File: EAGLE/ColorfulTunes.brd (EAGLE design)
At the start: 160 x 100 mm, 6 parts, among them U1 0.56_HEX_BACKPACK

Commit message: Please check this schematic :)
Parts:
- added CS1: COLOR_SENSOR_PINS, ColorfulTunes:COLOR_SENSOR
- added R4, R5, R6, R7: (no value), ColorfulTunes:R0402
- added R8: POTENTIOMETER, ColorfulTunes:POT-PO90S
- added SERVO1: SERVO_PINS, ColorfulTunes:SERVO_PINS
- added USB1: USB_BOI, ColorfulTunes:USB_BOI
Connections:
- removed net RGB_PWR: D1.1, U$1.59
- removed net SYS.5V: U$1.24
- removed net SYS.5V_1: U$1.49
- removed net SYS.GND_1: U$1.22
- removed net SYS.GND_3: U$1.51
- removed net SYS_VIN: U$1.1
- removed net VCC: U1.VCC
- new net AIN_1V8.0: R8.S, U$1.19
- new net AIN_1V8.REF+: R8.CCW, U$1.18
- new net AIN_1V8.REF-: R8.CW, U$1.17
- new net GND: CS1.GND, SERVO1.P$1, U$1.16, U$1.22, U$1.51, U$1.57, U1.GND
- new net I2C1.SCL: CS1.SCL, R7.1, U$1.45
- new net I2C1.SDA: CS1.SDA, R6.1, U$1.47
- new net I2C2.SCL: R4.1, U$1.28, U1.SCL
- new net I2C2.SDA: R5.1, U$1.26, U1.SDA
- new net N$4: U$1.3, U$1.5
- new net SERVO_PWM: SERVO1.P$3, U$1.36
- new net USB1.D+: U$1.11, USB1.D+
- new net USB1.D-: U$1.9, USB1.D-
- new net USB1.GND: U$1.13, U$1.15, USB1.GND
- new net USB1.VIN: U$1.7, USB1.5V
- new net VDD_3P3V: D1.1, R4.2, R5.2, R6.2, R7.2, U$1.14, U$1.59
- new net VDD_5V: CS1.VIN, SERVO1.P$2, U$1.1, U$1.24, U$1.49, U1.VCC
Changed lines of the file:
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@@
 <attribute name="VALUE" x="-60.96" y="38.1" size="1.27" layer="27"/>
 </element>
+<element name="R4" library="ColorfulTunes" package="R0402" value="" x="-68.58" y="-2.54" smashed="yes">
+<attribute name="NAME" x="-69.469" y="-2.032" size="0.8128" layer="25"/>
+<attribute name="VALUE" x="-69.469" y="-3.302" size="0.254" layer="27"/>
+</element>
+<element name="R5" library="ColorfulTunes" package="R0402" value="" x="-68.58" y="-6.35" smashed="yes">
+<attribute name="NAME" x="-69.469" y="-5.842" size="0.8128" layer="25"/>
+<attribute name="VALUE" x="-69.469" y="-7.112" size="0.254" layer="27"/>
+</element>
+<element name="CS1" library="ColorfulTunes" package="COLOR_SENSOR" value="COLOR_SENSOR_PINS" x="-67.31" y="-10.16" smashed="yes"/>
+<element name="R6" library="ColorfulTunes" package="R0402" value="" x="-68.58" y="-13.97" smashed="yes">
+<attribute name="NAME" x="-69.469" y="-13.462" size="0.8128" layer="25"/>
+<attribute name="VALUE" x="-69.469" y="-14.732" size="0.254" layer="27"/>
+</element>
+<element name="R7" library="ColorfulTunes" package="R0402" value="" x="-68.58" y="-17.78" smashed="yes">
+<attribute name="NAME" x="-69.469" y="-17.272" size="0.8128" layer="25"/>
+<attribute name="VALUE" x="-69.469" y="-18.542" size="0.254" layer="27"/>
+</element>
+<element name="USB1" library="ColorfulTunes" package="USB_BOI" value="USB_BOI" x="-80.01" y="-2.54" smashed="yes">
+<attribute name="NAME" x="-84.54" y="2.68" size="1.778" layer="25" font="vector" ratio="12"/>
+<attribute name="VALUE" x="-84.6" y="-18.18" size="1.778" layer="27" font="vector" ratio="12"/>
+</element>
+<element name="R8" library="ColorfulTunes" package="POT-PO90S" value="POTENTIOMETER" x="-95.25" y="-15.24" smashed="yes">
+<attribute name="NAME" x="-100.33" y="-2.54" size="0.8128" layer="25"/>
+<attribute name="VALUE" x="-100.33" y="-17.78" size="0.8128" layer="27"/>
+</element>
+<element name="SERVO1" library="ColorfulTunes" package="SERVO_PINS" value="SERVO_PINS" x="-96.52" y="-20.32" smashed="yes"/>
 </elements>
 <signals>
-<signal name="SYS_VIN">
-<contactref element="U$1" pad="1"/>
-</signal>
-<signal name="SYS.GND_1">
-<contactref element="U$1" pad="22"/>
-</signal>
-<signal name="SYS.5V">
-<contactref element="U$1" pad="24"/>
-</signal>
-<signal name="SYS.GND_3">
-<contactref element="U$1" pad="51"/>
-</signal>
-<signal name="SYS.5V_1">
-<contactref element="U$1" pad="49"/>
-</signal>
-<signal name="VCC">
-<contactref element="U1" pad="VCC"/>
-</signal>
-<signal name="RGB_PWR">
-<contactref element="D1" pad="1"/>
-<contactref element="U$1" pad="59"/>
-<wire x1="-35.814" y1="29.21" x2="-66.81" y2="43.17" width="0" layer="19" extent="1-1"/>
-</signal>
 <signal name="N$1">
 <contactref element="R1" pad="1"/>
@@
 <wire x1="-51.5112" y1="71.12" x2="-61.214" y2="29.21" width="0" layer="19" extent="1-1"/>
 </signal>
+<signal name="VDD_3P3V">
+<contactref element="D1" pad="1"/>
+<contactref element="R4" pad="2"/>
+<contactref element="U$1" pad="59"/>
+<contactref element="U$1" pad="14"/>
+<contactref element="R5" pad="2"/>
+<contactref element="R6" pad="2"/>
+<contactref element="R7" pad="2"/>
+<wire x1="-68.0212" y1="-13.97" x2="-68.0212" y2="-17.78" width="0" layer="19" extent="1-1"/>
+<wire x1="-68.0212" y1="-6.35" x2="-68.0212" y2="-13.97" width="0" layer="19" extent="1-1"/>
+<wire x1="-68.0212" y1="-2.54" x2="-68.0212" y2="-6.35" width="0" layer="19" extent="1-1"/>
+<wire x1="-48.514" y1="9.398" x2="-68.0212" y2="-2.54" width="0" layer="19" extent="1-1"/>
+<wire x1="-35.814" y1="29.21" x2="-48.514" y2="9.398" width="0" layer="19" extent="1-1"/>
+<wire x1="-66.81" y1="43.17" x2="-35.814" y2="29.21" width="0" layer="19" extent="1-1"/>
+</signal>
+<signal name="VDD_5V">
+<contactref element="U1" pad="VCC"/>
+<contactref element="U$1" pad="24"/>
+<contactref element="U$1" pad="49"/>
+<contactref element="U$1" pad="1"/>
+<contactref element="CS1" pad="VIN"/>
+<contactref element="SERVO1" pad="P$2"/>
+<wire x1="-63.754" y1="6.858" x2="-96.52" y2="-20.32" width="0" layer="19" extent="1-1"/>
+<wire x1="-52.07" y1="-10.16" x2="-63.754" y2="6.858" width="0" layer="19" extent="1-1"/>
+<wire x1="-35.814" y1="9.398" x2="-52.07" y2="-10.16" width="0" layer="19" extent="1-1"/>
+<wire x1="-48.514" y1="29.21" x2="-35.814" y2="9.398" width="0" layer="19" extent="1-1"/>
+<wire x1="-34.036" y1="64.77" x2="-48.514" y2="29.21" width="0" layer="19" extent="1-1"/>
+</signal>
+<signal name="I2C2.SCL">
+<contactref element="U$1" pad="28"/>
+<contactref element="R4" pad="1"/>
+<contactref element="U1" pad="SCL"/>
+<wire x1="-30.734" y1="9.398" x2="-69.1388" y2="-2.54" width="0" layer="19" extent="1-1"/>
+<wire x1="-41.656" y1="64.77" x2="-30.734" y2="9.398" width="0" layer="19" extent="1-1"/>
+</signal>
+<signal name="I2C2.SDA">
+<contactref element="U$1" pad="26"/>
+<contactref element="U1" pad="SDA"/>
+<contactref element="R5" pad="1"/>
+<wire x1="-33.274" y1="9.398" x2="-69.1388" y2="-6.35" width="0" layer="19" extent="1-1"/>
+<wire x1="-39.116" y1="64.77" x2="-33.274" y2="9.398" width="0" layer="19" extent="1-1"/>
+</signal>
+<signal name="GND">
+<contactref element="U$1" pad="57"/>
+<contactref element="U$1" pad="16"/>
+<contactref element="U$1" pad="51"/>
+<contactref element="U$1" pad="22"/>
+<contactref element="U1" pad="GND"/>
+<contactref element="CS1" pad="GND"/>
+<contactref element="SERVO1" pad="P$1"/>
+<wire x1="-54.61" y1="-10.16" x2="-99.06" y2="-20.32" width="0" layer="19" extent="1-1"/>
+<wire x1="-45.974" y1="9.398" x2="-54.61" y2="-10.16" width="0" layer="19" extent="1-1"/>
+<wire x1="-38.354" y1="9.398" x2="-45.974" y2="9.398" width="0" layer="19" extent="1-1"/>
+<wire x1="-45.974" y1="29.21" x2="-45.974" y2="9.398" width="0" layer="19" extent="1-1"/>
+<wire x1="-38.354" y1="29.21" x2="-45.974" y2="29.21" width="0" layer="19" extent="1-1"/>
+<wire x1="-36.576" y1="64.77" x2="-38.354" y2="29.21" width="0" layer="19" extent="1-1"/>
+</signal>
+<signal name="I2C1.SDA">
+<contactref element="CS1" pad="SDA"/>
+<contactref element="R6" pad="1"/>
+<contactref element="U$1" pad="47"/>
+<wire x1="-62.23" y1="-10.16" x2="-69.1388" y2="-13.97" width="0" layer="19" extent="1-1"/>
+<wire x1="-51.054" y1="29.21" x2="-62.23" y2="-10.16" width="0" layer="19" extent="1-1"/>
+</signal>
+<signal name="I2C1.SCL">
+<contactref element="CS1" pad="SCL"/>
+<contactref element="R7" pad="1"/>
+<contactref element="U$1" pad="45"/>
+<wire x1="-59.69" y1="-10.16" x2="-69.1388" y2="-17.78" width="0" layer="19" extent="1-1"/>
+<wire x1="-53.594" y1="29.21" x2="-59.69" y2="-10.16" width="0" layer="19" extent="1-1"/>
+</signal>
+<signal name="USB1.GND">
+<contactref element="USB1" pad="GND"/>
+<contactref element="U$1" pad="13"/>
+<contactref element="U$1" pad="15"/>
+<wire x1="-48.514" y1="6.858" x2="-76.51" y2="-2.54" width="0" layer="19" extent="1-1"/>
+<wire x1="-45.974" y1="6.858" x2="-48.514" y2="6.858" width="0" layer="19" extent="1-1"/>
+</signal>
+<signal name="USB1.D+">
+<contactref element="USB1" pad="D+"/>
+<contactref element="U$1" pad="11"/>
+<wire x1="-51.054" y1="6.858" x2="-79.01" y2="-2.54" width="0" layer="19" extent="1-1"/>
+</signal>
+<signal name="USB1.D-">
+<contactref element="USB1" pad="D-"/>
+<contactref element="U$1" pad="9"/>
+<wire x1="-53.594" y1="6.858" x2="-81.01" y2="-2.54" width="0" layer="19" extent="1-1"/>
+</signal>
+<signal name="USB1.VIN">
+<contactref element="USB1" pad="5V"/>
+<contactref element="U$1" pad="7"/>
+<wire x1="-56.134" y1="6.858" x2="-83.51" y2="-2.54" width="0" layer="19" extent="1-1"/>
+</signal>
+<signal name="N$4">
+<contactref element="U$1" pad="3"/>
+<contactref element="U$1" pad="5"/>
+<wire x1="-58.674" y1="6.858" x2="-61.214" y2="6.858" width="0" layer="19" extent="1-1"/>
+</signal>
+<signal name="AIN_1V8.0">
+<contactref element="R8" pad="S"/>
+<contactref element="U$1" pad="19"/>
+<wire x1="-40.894" y1="6.858" x2="-95.25" y2="-15.24" width="0" layer="19" extent="1-1"/>
+</signal>
+<signal name="AIN_1V8.REF+">
+<contactref element="R8" pad="CCW"/>
+<contactref element="U$1" pad="18"/>
+<wire x1="-43.434" y1="9.398" x2="-97.75" y2="-15.24" width="0" layer="19" extent="1-1"/>
+</signal>
+<signal name="AIN_1V8.REF-">
+<contactref element="R8" pad="CW"/>
+<contactref element="U$1" pad="17"/>
+<wire x1="-43.434" y1="6.858" x2="-92.75" y2="-15.24" width="0" layer="19" extent="1-1"/>
+</signal>
+<signal name="SERVO_PWM">
+<contactref element="SERVO1" pad="P$3"/>
+<contactref element="U$1" pad="36"/>
+<wire x1="-20.574" y1="9.398" x2="-93.98" y2="-20.32" width="0" layer="19" extent="1-1"/>
+</signal>
 </signals>

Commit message: Found some mistakes, please check this one. Thank you!
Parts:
- R1, R2, R3: value (none) -> 470 M
- R4, R6, R7: value (none) -> 2.2 k
- R5: value (none) -> 2.2k
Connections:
- new net SYS.5V_1: U$1.49
- net VDD_5V: no longer U$1.49
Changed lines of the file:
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@@
 <attribute name="VALUE" x="-68.31" y="37.67" size="0.8128" layer="27" font="vector" ratio="12"/>
 </element>
-<element name="R1" library="ColorfulTunes" package="R0402" value="" x="-46.99" y="71.12" smashed="yes">
+<element name="R1" library="ColorfulTunes" package="R0402" value="470 M" x="-46.99" y="71.12" smashed="yes">
 <attribute name="NAME" x="-47.879" y="71.628" size="0.8128" layer="25"/>
 <attribute name="VALUE" x="-47.879" y="70.358" size="0.254" layer="27"/>
 </element>
-<element name="R2" library="ColorfulTunes" package="R0402" value="" x="-49.53" y="71.12" smashed="yes">
+<element name="R2" library="ColorfulTunes" package="R0402" value="470 M" x="-49.53" y="71.12" smashed="yes">
 <attribute name="NAME" x="-50.419" y="71.628" size="0.8128" layer="25"/>
 <attribute name="VALUE" x="-50.419" y="70.358" size="0.254" layer="27"/>
 </element>
-<element name="R3" library="ColorfulTunes" package="R0402" value="" x="-52.07" y="71.12" smashed="yes">
+<element name="R3" library="ColorfulTunes" package="R0402" value="470 M" x="-52.07" y="71.12" smashed="yes">
 <attribute name="NAME" x="-52.959" y="71.628" size="0.8128" layer="25"/>
 <attribute name="VALUE" x="-52.959" y="70.358" size="0.254" layer="27"/>
@@
 <attribute name="VALUE" x="-60.96" y="38.1" size="1.27" layer="27"/>
 </element>
-<element name="R4" library="ColorfulTunes" package="R0402" value="" x="-68.58" y="-2.54" smashed="yes">
+<element name="R4" library="ColorfulTunes" package="R0402" value="2.2 k" x="-68.58" y="-2.54" smashed="yes">
 <attribute name="NAME" x="-69.469" y="-2.032" size="0.8128" layer="25"/>
 <attribute name="VALUE" x="-69.469" y="-3.302" size="0.254" layer="27"/>
 </element>
-<element name="R5" library="ColorfulTunes" package="R0402" value="" x="-68.58" y="-6.35" smashed="yes">
+<element name="R5" library="ColorfulTunes" package="R0402" value="2.2k" x="-68.58" y="-6.35" smashed="yes">
 <attribute name="NAME" x="-69.469" y="-5.842" size="0.8128" layer="25"/>
 <attribute name="VALUE" x="-69.469" y="-7.112" size="0.254" layer="27"/>
 </element>
 <element name="CS1" library="ColorfulTunes" package="COLOR_SENSOR" value="COLOR_SENSOR_PINS" x="-67.31" y="-10.16" smashed="yes"/>
-<element name="R6" library="ColorfulTunes" package="R0402" value="" x="-68.58" y="-13.97" smashed="yes">
+<element name="R6" library="ColorfulTunes" package="R0402" value="2.2 k" x="-68.58" y="-13.97" smashed="yes">
 <attribute name="NAME" x="-69.469" y="-13.462" size="0.8128" layer="25"/>
 <attribute name="VALUE" x="-69.469" y="-14.732" size="0.254" layer="27"/>
 </element>
-<element name="R7" library="ColorfulTunes" package="R0402" value="" x="-68.58" y="-17.78" smashed="yes">
+<element name="R7" library="ColorfulTunes" package="R0402" value="2.2 k" x="-68.58" y="-17.78" smashed="yes">
 <attribute name="NAME" x="-69.469" y="-17.272" size="0.8128" layer="25"/>
 <attribute name="VALUE" x="-69.469" y="-18.542" size="0.254" layer="27"/>
@@
 </elements>
 <signals>
-<signal name="N$1">
-<contactref element="R1" pad="1"/>
-<contactref element="D1" pad="2"/>
-<wire x1="-65.31" y1="43.17" x2="-47.5488" y2="71.12" width="0" layer="19" extent="1-1"/>
-</signal>
 <signal name="N$2">
 <contactref element="R2" pad="1"/>
 <contactref element="D1" pad="3"/>
 <wire x1="-50.0888" y1="71.12" x2="-65.31" y2="40.07" width="0" layer="19" extent="1-1"/>
-</signal>
-<signal name="N$3">
-<contactref element="R3" pad="1"/>
-<contactref element="D1" pad="4"/>
-<wire x1="-52.6288" y1="71.12" x2="-66.81" y2="40.07" width="0" layer="19" extent="1-1"/>
 </signal>
 <signal name="B">
@@
 <contactref element="U1" pad="VCC"/>
 <contactref element="U$1" pad="24"/>
-<contactref element="U$1" pad="49"/>
 <contactref element="U$1" pad="1"/>
 <contactref element="CS1" pad="VIN"/>
@@
 <wire x1="-52.07" y1="-10.16" x2="-63.754" y2="6.858" width="0" layer="19" extent="1-1"/>
 <wire x1="-35.814" y1="9.398" x2="-52.07" y2="-10.16" width="0" layer="19" extent="1-1"/>
-<wire x1="-48.514" y1="29.21" x2="-35.814" y2="9.398" width="0" layer="19" extent="1-1"/>
-<wire x1="-34.036" y1="64.77" x2="-48.514" y2="29.21" width="0" layer="19" extent="1-1"/>
+<wire x1="-34.036" y1="64.77" x2="-35.814" y2="9.398" width="0" layer="19" extent="1-1"/>
 </signal>
 <signal name="I2C2.SCL">
@@
 <wire x1="-20.574" y1="9.398" x2="-93.98" y2="-20.32" width="0" layer="19" extent="1-1"/>
 </signal>
+<signal name="N$1">
+<contactref element="D1" pad="2"/>
+<contactref element="R1" pad="1"/>
+<wire x1="-65.31" y1="43.17" x2="-47.5488" y2="71.12" width="0" layer="19" extent="1-1"/>
+</signal>
+<signal name="N$3">
+<contactref element="D1" pad="4"/>
+<contactref element="R3" pad="1"/>
+<wire x1="-52.6288" y1="71.12" x2="-66.81" y2="40.07" width="0" layer="19" extent="1-1"/>
+</signal>
+<signal name="SYS.5V_1">
+<contactref element="U$1" pad="49"/>
+</signal>
 </signals>

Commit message: Am I really done? Is there really justice in this cold dark world?
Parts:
- added SW1: SLIDE_SWITCH, ColorfulTunes:JS202011SCQN
- moved USB1 172.4 mm to (78.7, 64.8), flipped to the bottom
- moved R8 150.5 mm to (31.2, 66.3)
- moved SERVO1 141.8 mm to (29.7, 44.2), flipped to the bottom, turned to 180 degrees
- moved U$1 139.6 mm to (59.7, 53.3), flipped to the bottom
- moved R7 136.6 mm to (49.5, 50.8), flipped to the bottom, turned to 90 degrees
- moved R6 132.5 mm to (47.0, 50.8), flipped to the bottom, turned to 90 degrees
- moved CS1 117.6 mm to (38.1, 41.9), flipped to the bottom, turned to 180 degrees
- moved D1 103.2 mm to (35.6, 47.0)
- moved R5 101.1 mm to (22.9, 36.8), turned to 90 degrees
- moved R4 97.4 mm to (20.6, 36.6), turned to 90 degrees
- moved R3 95.2 mm to (40.6, 49.5), turned to 90 degrees
- moved R2 93.3 mm to (40.6, 47.0), turned to 90 degrees
- moved R1 89.4 mm to (40.6, 53.3), turned to 90 degrees
- moved U1 75.5 mm to (29.2, 19.1)
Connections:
- removed net SYS.5V_1: U$1.49
- removed net USB1.GND: U$1.13, U$1.15, USB1.GND
- new net PRU0.6: SW1.2, SW1.5, U$1.64
- new net SYS_VIN: U$1.1
- net GND: now also SERVO1.1, SW1.3, SW1.6, U$1.13, U$1.15, USB1.GND; no longer SERVO1.P$1
- net SERVO_PWM: now also SERVO1.3; no longer SERVO1.P$3
- net VDD_3P3V: now also SW1.1, SW1.4
- net VDD_5V: now also SERVO1.2, U$1.49; no longer SERVO1.P$2, U$1.1
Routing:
- net G: track 0.00 -> 111.6 mm
- net R: track 0.00 -> 111.2 mm
- net PRU0.6: track 0.00 -> 46.1 mm
- net I2C1.SCL: track 0.00 -> 44.2 mm
- net I2C1.SDA: track 0.00 -> 44.0 mm
- net USB1.D+: track 0.00 -> 41.4 mm, vias 0 -> 1
- net USB1.D-: track 0.00 -> 41.3 mm, vias 0 -> 1
- net USB1.VIN: track 0.00 -> 40.8 mm, vias 0 -> 1
- net I2C2.SDA: track 0.00 -> 37.9 mm, vias 0 -> 1
- net I2C2.SCL: track 0.00 -> 37.1 mm, vias 0 -> 1
- net B: track 0.00 -> 31.6 mm
- net SERVO_PWM: track 0.00 -> 29.9 mm, vias 0 -> 1
- net VDD_5V: track 0.00 -> 24.7 mm, vias 0 -> 2
- net VDD_3P3V: track 0.00 -> 18.2 mm, vias 0 -> 8
- net AIN_1V8.REF+: track 0.00 -> 9.96 mm
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- added copper zone on layer 2, net GND
- added copper zone on layer 15, net VDD_3P3V
- added copper zone on layer 15, net VDD_5V
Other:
- board size 160 x 100 mm -> 91.4 x 90.2 mm

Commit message: Almost there!
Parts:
- added FUD1, FUD2, FUD3: FIDUCIAL, ColorfulTunes:FIDUCIAL_40MIL
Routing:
- net VDD_3P3V: track 18.2 -> 15.9 mm, vias 8 -> 7
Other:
- board text added: "COLORFUL TUNES"
- board text added: "JFTA"
- board text added: "REV. 1"

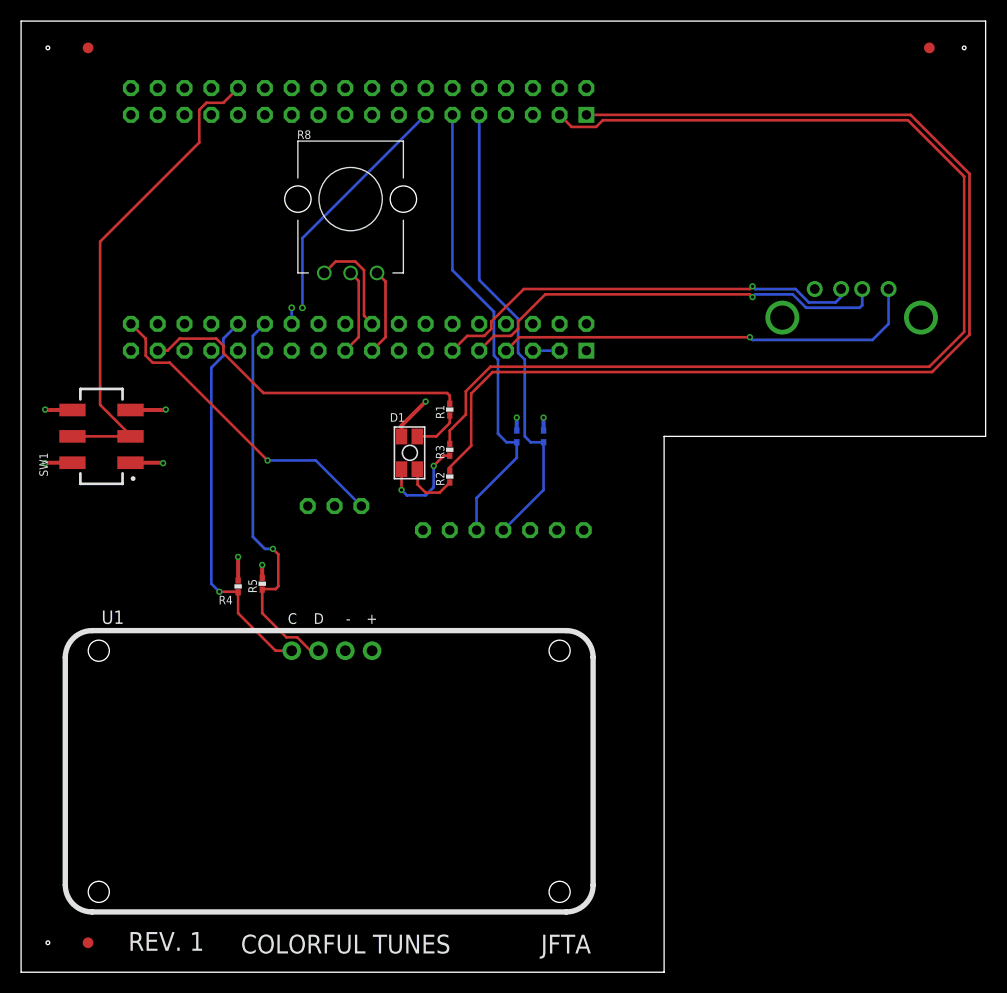
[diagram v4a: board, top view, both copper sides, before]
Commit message: with the mounting holes
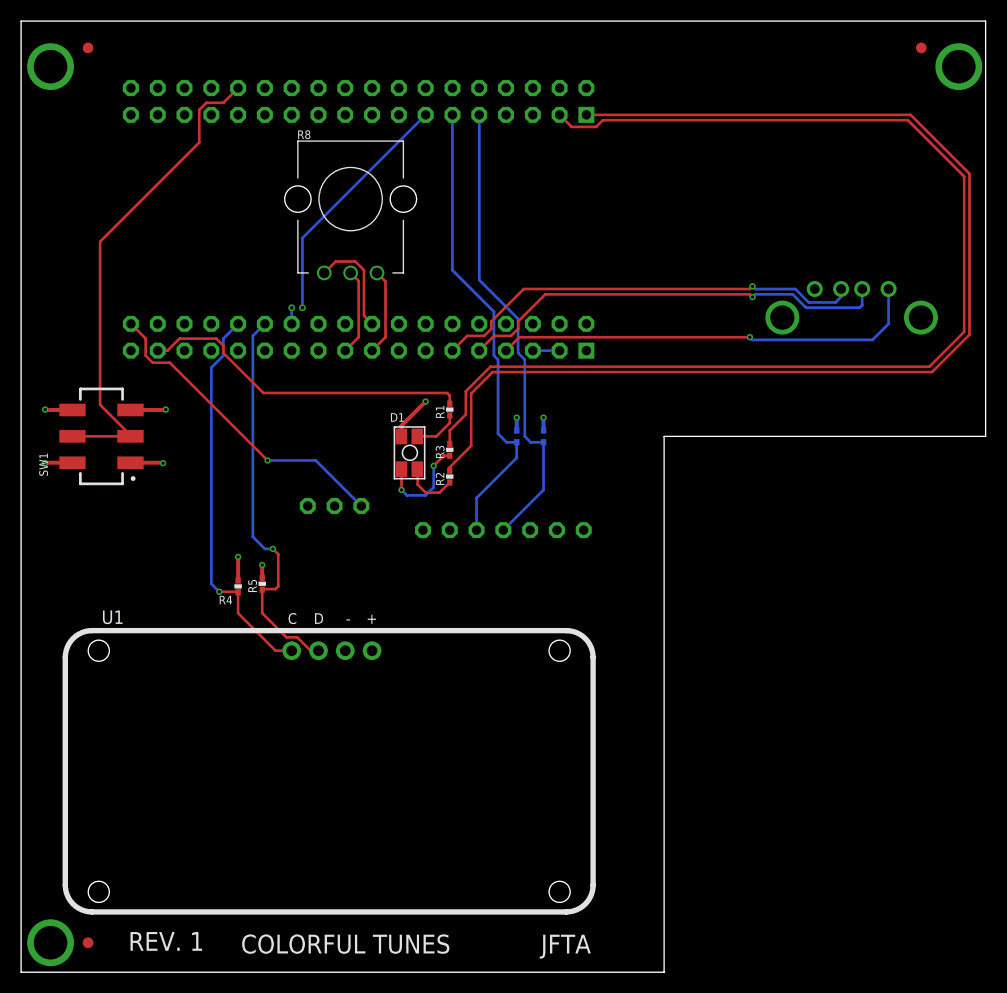
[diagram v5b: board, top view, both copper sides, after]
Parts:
- added MGT1, MGT2, MGT3: MOUNTING_HOLE, ColorfulTunes:MOUNTING_HOLE
- moved FUD3 0.76 mm to (85.3, 87.6)
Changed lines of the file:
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@@
 <wire x1="0" y1="90.17" x2="0" y2="0" width="0" layer="20"/>
 <text x="49.276" y="1.778" size="1.778" layer="25" font="vector" ratio="12">JFTA</text>
-<hole x="2.54" y="2.794" drill="0.35"/>
-<hole x="2.54" y="87.63" drill="0.35"/>
-<hole x="89.408" y="87.63" drill="0.35"/>
 <text x="20.828" y="1.778" size="1.778" layer="25" font="vector" distance="12">COLORFUL TUNES</text>
 <text x="10.16" y="2.032" size="1.778" layer="25" font="vector" ratio="12">REV. 1</text>
@@
 <element name="FUD1" library="ColorfulTunes" package="FIDUCIAL_40MIL" value="FIDUCIAL" x="6.35" y="2.794" smashed="yes"/>
 <element name="FUD2" library="ColorfulTunes" package="FIDUCIAL_40MIL" value="FIDUCIAL" x="6.35" y="87.63" smashed="yes"/>
-<element name="FUD3" library="ColorfulTunes" package="FIDUCIAL_40MIL" value="FIDUCIAL" x="86.106" y="87.63" smashed="yes"/>
+<element name="FUD3" library="ColorfulTunes" package="FIDUCIAL_40MIL" value="FIDUCIAL" x="85.344" y="87.63" smashed="yes"/>
+<element name="MGT1" library="ColorfulTunes" package="MOUNTING_HOLE" value="MOUNTING_HOLE" x="2.794" y="2.794" smashed="yes"/>
+<element name="MGT2" library="ColorfulTunes" package="MOUNTING_HOLE" value="MOUNTING_HOLE" x="2.794" y="85.852" smashed="yes"/>
+<element name="MGT3" library="ColorfulTunes" package="MOUNTING_HOLE" value="MOUNTING_HOLE" x="88.9" y="85.852" smashed="yes"/>
 </elements>
 <signals>
